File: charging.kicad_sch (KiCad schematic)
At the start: 23 parts, among them IC1 APX803S-31SA-7, J2 10164359-00011LF, Q1 BSS806NEH6327XTSA1, Q2 DMG2305UX, SW3 Power Switch, U3 MIC5365-3.3YC5-TR, U4 MCP73832

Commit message: added test points
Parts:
- added TP7: VBUS, TestPoint:TestPoint_Pad_1.0x1.0mm, symbol Connector:TestPoint
- added TP8: BATT, TestPoint:TestPoint_Pad_1.0x1.0mm, symbol Connector:TestPoint
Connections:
- net +BATT: now also TP8.1
- net VBUS: now also TP7.1
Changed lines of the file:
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@@
 	)
 	(junction
+		(at 66.04 68.58)
+		(diameter 0)
+		(color 0 0 0 0)
+	)
+	(junction
 		(at 59.69 128.27)
 		(diameter 0)
@@
 	)
 	(symbol
+		(lib_id "Connector:TestPoint")
+		(at 66.04 68.58 270)
+		(unit 1)
+		(exclude_from_sim no)
+		(in_bom yes)
+		(on_board yes)
+		(dnp no)
+		(fields_autoplaced yes)
+		(property "Reference" "TP7"
+			(at 71.12 67.3099 90)
+			(effects
+				(font
+					(size 1.27 1.27)
+				)
+				(justify left)
+			)
+		)
+		(property "Value" "VBUS"
+			(at 71.12 69.8499 90)
+			(effects
+				(font
+					(size 1.27 1.27)
+				)
+				(justify left)
+			)
+		)
+		(property "Footprint" "TestPoint:TestPoint_Pad_1.0x1.0mm"
+			(at 66.04 73.66 0)
+			(effects
+				(font
+					(size 1.27 1.27)
+				)
+				(hide yes)
+			)
+		)
+		(property "Datasheet" "~"
+			(at 66.04 73.66 0)
+			(effects
+				(font
+					(size 1.27 1.27)
+				)
+				(hide yes)
+			)
+		)
+		(property "Description" "test point"
+			(at 66.04 68.58 0)
+			(effects
+				(font
+					(size 1.27 1.27)
+				)
+				(hide yes)
+			)
+		)
+		(pin "1"
+		)
+		(instances
+			(project ""
+				(path "/5c9eb70e-53a3-4f57-8f37-8853f9cac53c/b9b17dec-f84f-4841-bdb5-cbe0cc549f61"
+					(reference "TP7")
+					(unit 1)
+				)
+			)
+		)
+	)
+	(symbol
 		(lib_id "MIC5365-3.3YC5-TR:MIC5365-3.3YC5-TR")
 		(at 184.15 77.47 0)
@@
 					(unit 1)
 				)
+			)
+		)
+	)
+	(symbol
+		(lib_id "Connector:TestPoint")
+		(at 31.75 111.76 90)
+		(unit 1)
+		(exclude_from_sim no)
+		(in_bom yes)
+		(on_board yes)
+		(dnp no)
+		(fields_autoplaced yes)
+		(property "Reference" "TP8"
+			(at 28.448 106.68 90)
+			(effects
+				(font
+					(size 1.27 1.27)
+				)
+			)
+		)
+		(property "Value" "BATT"
+			(at 28.448 109.22 90)
+			(effects
+				(font
+					(size 1.27 1.27)
+				)
+			)
+		)
+		(property "Footprint" "TestPoint:TestPoint_Pad_1.0x1.0mm"
+			(at 31.75 106.68 0)
+			(effects
+				(font
+					(size 1.27 1.27)
+				)
+				(hide yes)
+			)
+		)
+		(property "Datasheet" "~"
+			(at 31.75 106.68 0)
+			(effects
+				(font
+					(size 1.27 1.27)
+				)
+				(hide yes)
+			)
+		)
+		(property "Description" "test point"
+			(at 31.75 111.76 0)
+			(effects
+				(font
+					(size 1.27 1.27)
+				)
+				(hide yes)
+			)
+		)
+		(pin "1"
+		)
+		(instances
+			(project "bookbuddy_pcb"
+				(path "/5c9eb70e-53a3-4f57-8f37-8853f9cac53c/b9b17dec-f84f-4841-bdb5-cbe0cc549f61"
+					(reference "TP8")
+					(unit 1)
+				)

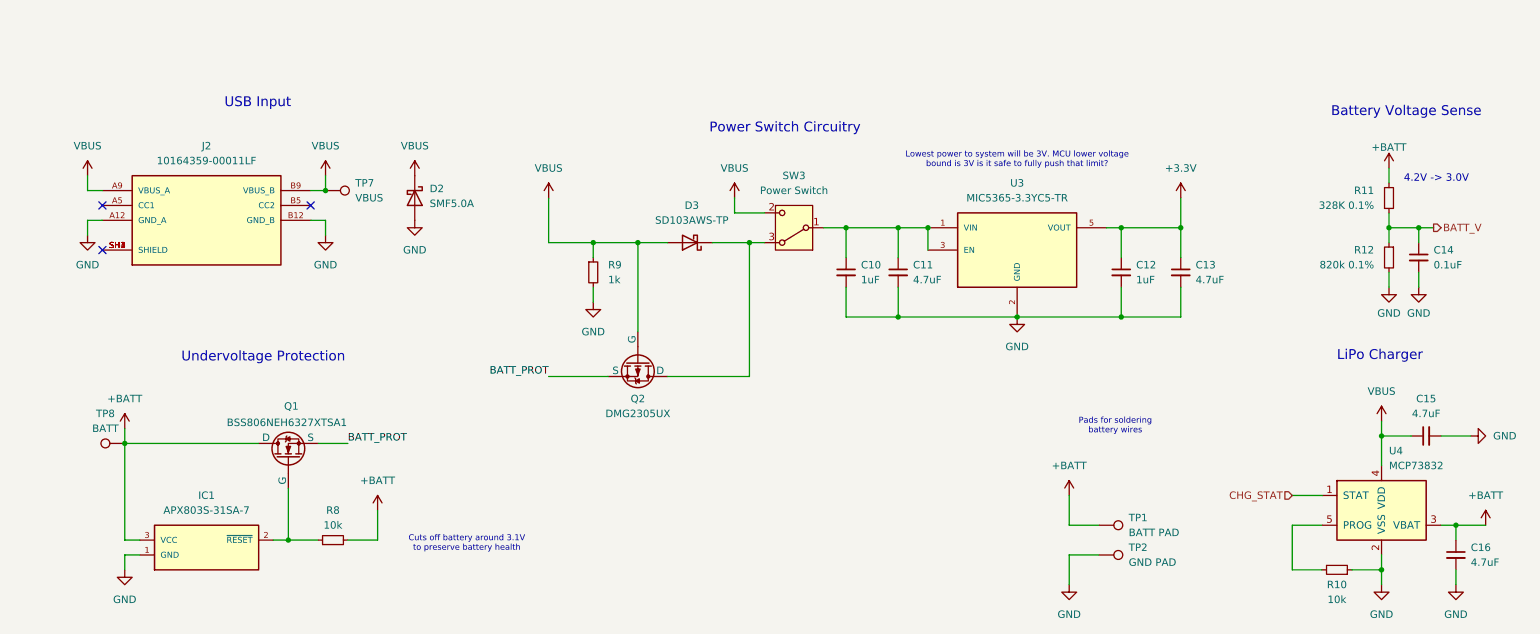
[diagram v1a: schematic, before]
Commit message: Made changes up to diode logic
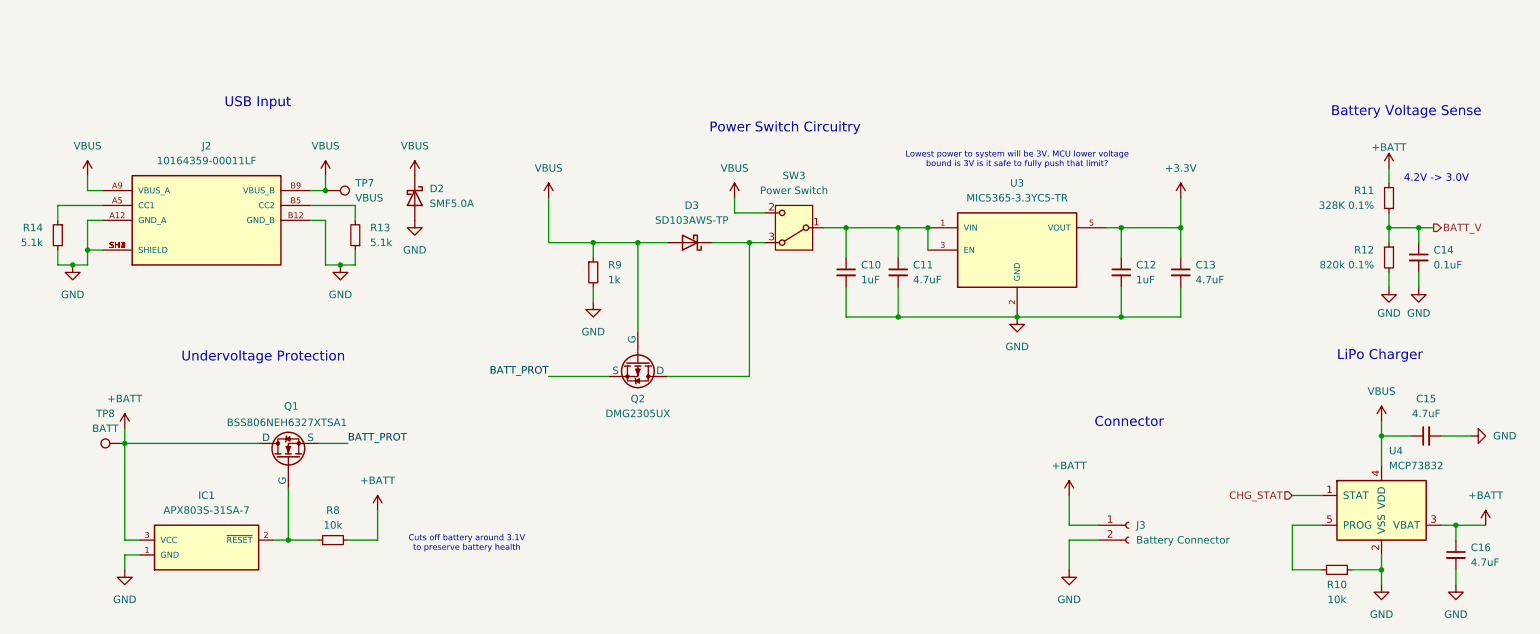
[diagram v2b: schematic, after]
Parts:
- removed TP1: BATT PAD, TestPoint:TestPoint_Pad_1.5x1.5mm, symbol Connector:TestPoint
- removed TP2: GND PAD, TestPoint:TestPoint_Pad_1.5x1.5mm, symbol Connector:TestPoint
- added J3: Battery Connector, bookbuddy:JST_S2B-PH-K-S_LF__SN_, symbol Connector:Conn_01x02_Socket
- added R13, R14: 5.1k, Resistor_SMD:R_0603_1608Metric_Pad0.98x0.95mm_HandSolder, symbol Device:R_Small
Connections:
- net +BATT: now also J3.1 (Pin_1)
- net GND: now also J2.SH1 (SHIELD), J2.SH2 (SHIELD), J2.SH3 (SHIELD), J2.SH4 (SHIELD), J3.2 (Pin_2), R13.1, R14.2
- net at J2.A5 (CC1): now also R14.1
- net at J2.B5 (CC2): now also R13.2
- no-connect marks 3 -> 0
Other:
- note added: "Connector"
- note removed: "Pads for soldering battery wires"

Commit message: made remaining changes to the schematic
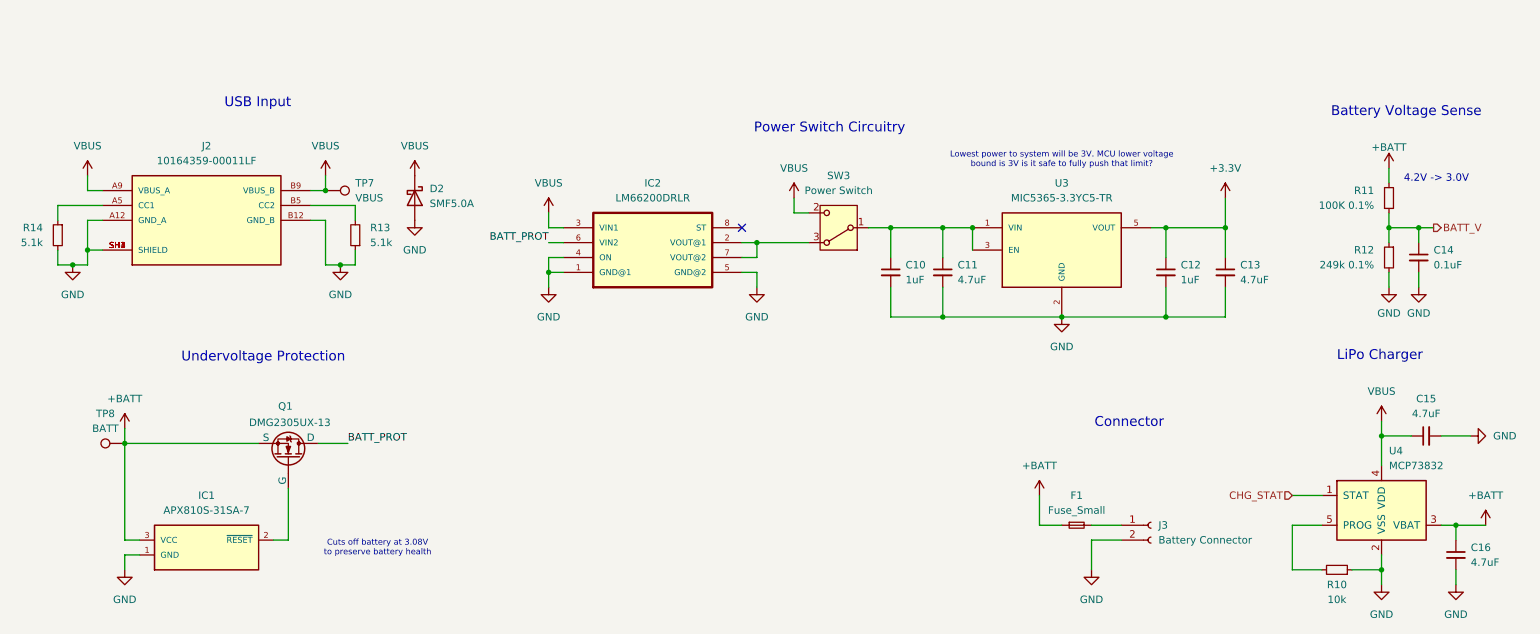
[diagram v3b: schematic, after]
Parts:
- removed D3: SD103AWS-TP, Diode_SMD:D_SOD-323, symbol Device:D_Schottky
- removed Q2: DMG2305UX, Package_TO_SOT_SMD:SOT-23-3, symbol Simulation_SPICE:PMOS
- removed R8: 10k, Resistor_SMD:R_0603_1608Metric_Pad0.98x0.95mm_HandSolder, symbol Device:R_Small
- removed R9: 1k, Resistor_SMD:R_0603_1608Metric_Pad0.98x0.95mm_HandSolder, symbol Device:R_Small
- added F1: Fuse_Small, symbol Device:Fuse_Small
- added IC2: LM66200DRLR, bookbuddy:SOT8, symbol LM66200DRLR:LM66200DRLR
- IC1: value APX803S-31SA-7 -> APX810S-31SA-7
- Q1: value BSS806NEH6327XTSA1 -> DMG2305UX-13
- R11: value 328K 0.1% -> 100K 0.1%
- R12: value 820k 0.1% -> 249k 0.1%
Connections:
- net +BATT: now also Q1.3 (S), F1.1; no longer J3.1 (Pin_1), Q1.1 (D)
- net BATT_PROT: now also Q1.1 (D), IC2.6 (VIN2); no longer Q1.3 (S)
- net GND: now also IC2.1 (GND@1), IC2.4 (ON), IC2.5 (GND@2)
- net VBUS: now also IC2.3 (VIN1)
- net at SW3.3 (A): now also IC2.2 (VOUT@1), IC2.7 (VOUT@2)
- new net: F1.2, J3.1 (Pin_1)
- no-connect marks 0 -> 1
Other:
- note added: "Cuts off battery at 3.08V to preserve battery health"
- note removed: "Cuts off battery around 3.1V to preserve battery health"
- moved on the sheet: C10, C11, C12, C13, J3, Q1, SW3, U3

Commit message: addressed Craig's comments
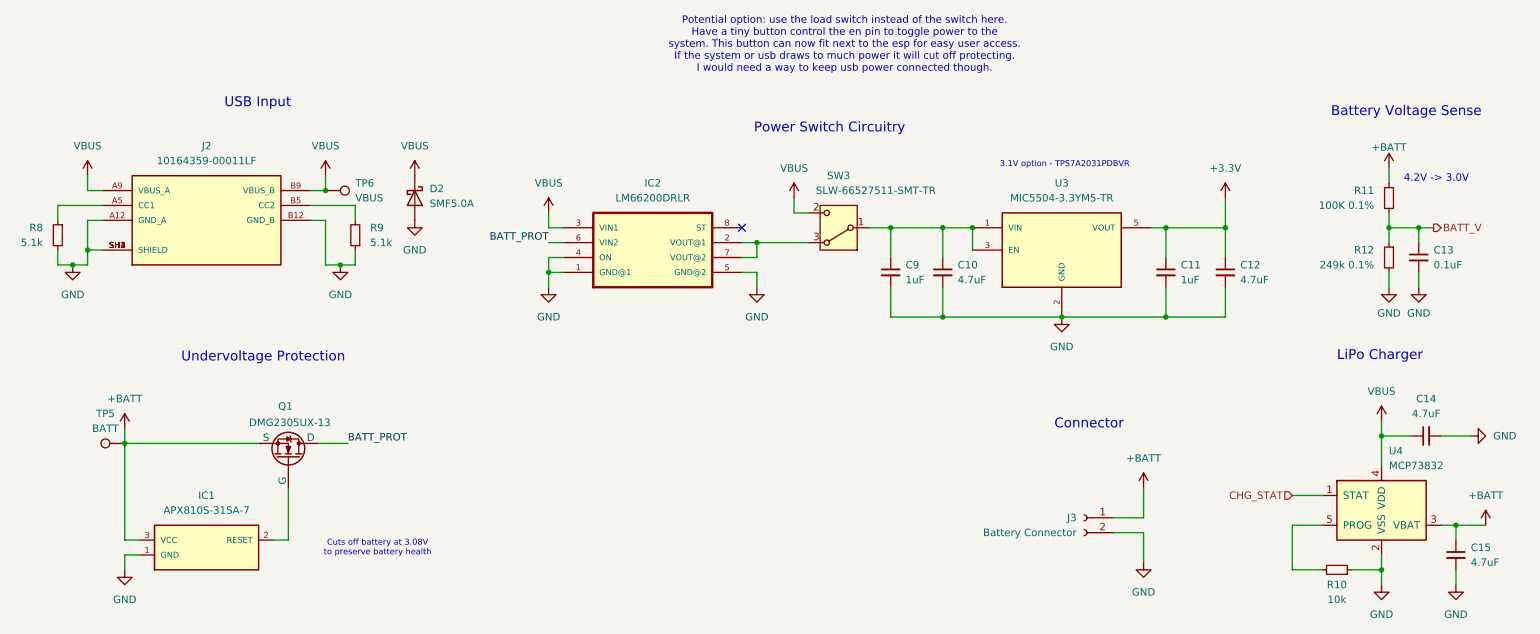
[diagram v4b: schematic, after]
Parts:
- removed F1: Fuse_Small, symbol Device:Fuse_Small
- SW3: value Power Switch -> SLW-66527511-SMT-TR; footprint bookbuddy:CUS-12B -> bookbuddy:SW_SLW-66527511-SMT-TR
- U3: value MIC5365-3.3YC5-TR -> MIC5504-3.3YM5-TR; footprint bookbuddy:SOT65P210X110-5N -> Package_TO_SOT_SMD:SOT-23-5_HandSoldering
- renumbered C11 to C10, C12 to C11, C13 to C12, C14 to C13, C15 to C14, C16 to C15, C10 to C9, R14 to R8, R13 to R9, TP8 to TP5, TP7 to TP6
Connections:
- net +BATT: now also J3.1 (Pin_1)
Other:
- note added: "3.1V option - TPS7A2031PDBVR"
- note added: "Potential option: use the load switch instead of the switch here. Have a tiny button control the en pin to toggle power to the system. This button can now fit next to the esp for easy user access. If the system or usb draws to much power it will cut off protecting. I would need a way to keep usb power connected though."
- note removed: "Lowest power to system will be 3V. MCU lower voltage bound is 3V is it safe to fully push that limit?"
- moved on the sheet: J3

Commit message: Added fuse
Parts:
- added F1: ERB-RD0R50X, bookbuddy:FUSC0402X49N, symbol Device:Fuse_Small
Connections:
- net +BATT: now also F1.2; no longer J3.1 (Pin_1)
- new net: F1.1, J3.1 (Pin_1)
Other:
- note added: "0.5A Rating"
- moved on the sheet: J3
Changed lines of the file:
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@@
 	(wire
 		(pts
-			(xy 205.74 127) (xy 205.74 132.08)
+			(xy 198.12 127) (xy 198.12 132.08)
 		)
 		(stroke
@@
 	(wire
 		(pts
-			(xy 200.66 127) (xy 205.74 127)
+			(xy 193.04 127) (xy 198.12 127)
+		)
+		(stroke
+			(width 0)
+			(type default)
+		)
+	)
+	(wire
+		(pts
+			(xy 193.04 124.46) (xy 195.58 124.46)
 		)
 		(stroke
@@
 		)
 	)
+	(text "0.5A Rating"
+		(exclude_from_sim no)
+		(at 187.198 117.856 0)
+		(effects
+			(font
+				(size 1.27 1.27)
+			)
+		)
+	)
 	(text "Power Switch Circuitry"
 		(exclude_from_sim no)
@@
 	(symbol
 		(lib_id "power:GND")
-		(at 205.74 132.08 0)
+		(at 198.12 132.08 0)
 		(mirror y)
 		(unit 1)
@@
 		(fields_autoplaced yes)
 		(property "Reference" "#PWR041"
-			(at 205.74 138.43 0)
+			(at 198.12 138.43 0)
 			(effects
 				(font
@@
 		)
 		(property "Value" "GND"
-			(at 205.74 137.16 0)
+			(at 198.12 137.16 0)
 			(effects
 				(font
@@
 		)
 		(property "Footprint" ""
-			(at 205.74 132.08 0)
+			(at 198.12 132.08 0)
 			(effects
 				(font
@@
 		)
 		(property "Datasheet" ""
-			(at 205.74 132.08 0)
+			(at 198.12 132.08 0)
 			(effects
 				(font
@@
 		)
 		(property "Description" "Power symbol creates a global label with name \"GND\" , ground"
-			(at 205.74 132.08 0)
+			(at 198.12 132.08 0)
 			(effects
 				(font
@@
 	(symbol
 		(lib_id "Connector:Conn_01x02_Socket")
-		(at 195.58 124.46 0)
+		(at 187.96 124.46 0)
 		(mirror y)
 		(unit 1)
@@
 		(fields_autoplaced yes)
 		(property "Reference" "J3"
-			(at 194.31 124.4599 0)
+			(at 186.69 124.4599 0)
 			(effects
 				(font
@@
 		)
 		(property "Value" "Battery Connector"
-			(at 194.31 126.9999 0)
+			(at 186.69 126.9999 0)
 			(effects
 				(font
@@
 		)
 		(property "Footprint" "bookbuddy:JST_S2B-PH-K-S_LF__SN_"
-			(at 195.58 124.46 0)
+			(at 187.96 124.46 0)
 			(effects
 				(font
@@
 		)
 		(property "Datasheet" "~"
-			(at 195.58 124.46 0)
+			(at 187.96 124.46 0)
 			(effects
 				(font
@@
 		)
 		(property "Description" "Generic connector, single row, 01x02, script generated"
-			(at 195.58 124.46 0)
+			(at 187.96 124.46 0)
 			(effects
 				(font
@@
 					(unit 1)
 				)
+			)
+		)
+	)
+	(symbol
+		(lib_id "Device:Fuse_Small")
+		(at 198.12 124.46 0)
+		(unit 1)
+		(exclude_from_sim no)
+		(in_bom yes)
+		(on_board yes)
+		(dnp no)
+		(fields_autoplaced yes)
+		(property "Reference" "F1"
+			(at 198.12 119.38 0)
+			(effects
+				(font
+					(size 1.27 1.27)
+				)
+			)
+		)
+		(property "Value" "ERB-RD0R50X"
+			(at 198.12 121.92 0)
+			(effects
+				(font
+					(size 1.27 1.27)
+				)
+			)
+		)
+		(property "Footprint" "bookbuddy:FUSC0402X49N"
+			(at 198.12 124.46 0)
+			(effects
+				(font
+					(size 1.27 1.27)
+				)
+				(hide yes)
+			)
+		)
+		(property "Datasheet" "~"
+			(at 198.12 124.46 0)
+			(effects
+				(font
+					(size 1.27 1.27)
+				)
+				(hide yes)
+			)
+		)
+		(property "Description" "Fuse, small symbol"
+			(at 198.12 124.46 0)
+			(effects
+				(font
+					(size 1.27 1.27)
+				)
+				(hide yes)
+			)
+		)
+		(pin "1"
+		)
+		(pin "2"
+		)
+		(instances
+			(project ""
+				(path "/5c9eb70e-53a3-4f57-8f37-8853f9cac53c/b9b17dec-f84f-4841-bdb5-cbe0cc549f61"
+					(reference "F1")
+					(unit 1)
+				)

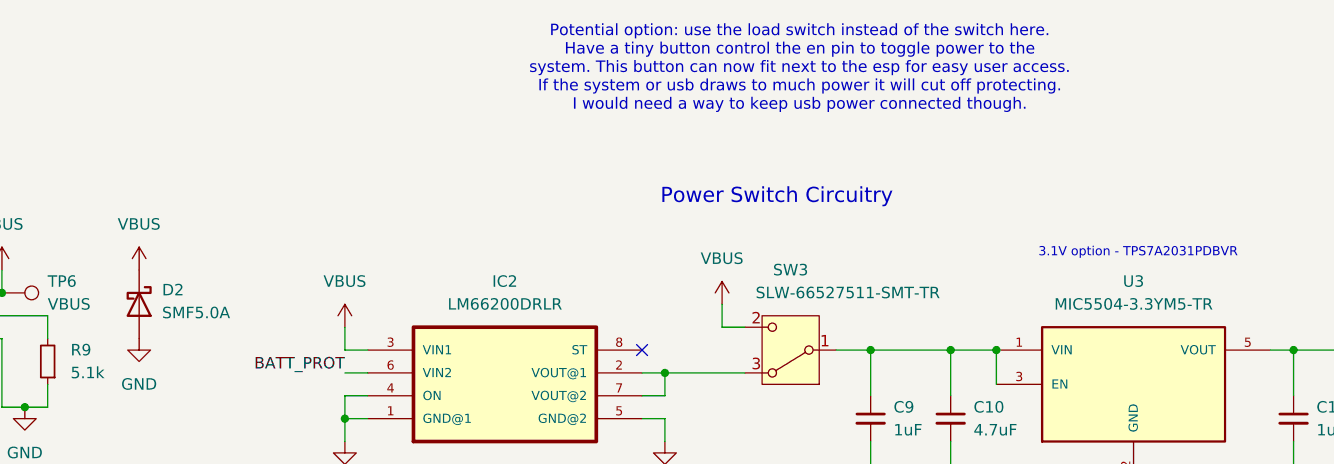
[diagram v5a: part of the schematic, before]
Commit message: finished routing the pcb
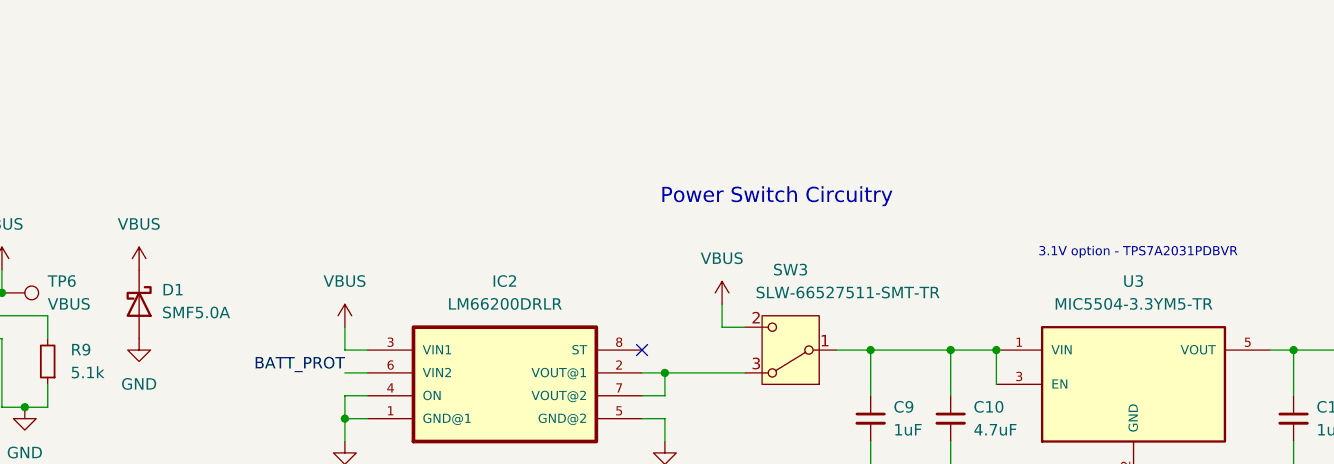
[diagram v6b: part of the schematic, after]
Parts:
- renumbered D2 to D1
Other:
- note removed: "Potential option: use the load switch instead of the switch here. Have a tiny button control the en pin to toggle power to the system. This button can now fit next to the esp for easy user access. If the system or usb draws to much power it will cut off protecting. I would need a way to keep usb power connected though."
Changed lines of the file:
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@@
-		)
-	)
-	(text "Potential option: use the load switch instead of the switch here.\nHave a tiny button control the en pin to toggle power to the\nsystem. This button can now fit next to the esp for easy user access.\nIf the system or usb draws to much power it will cut off protecting.\nI would need a way to keep usb power connected though.\n"
-		(exclude_from_sim no)
-		(at 154.686 43.688 0)
-		(effects
-			(font
-				(size 1.27 1.27)
-			)
 		)
 	)
@@
 		(dnp no)
 		(fields_autoplaced yes)
-		(property "Reference" "D2"
+		(property "Reference" "D1"
 			(at 83.82 68.2624 90)
 			(effects
@@
 			(project "bookbuddy_pcb"
 				(path "/5c9eb70e-53a3-4f57-8f37-8853f9cac53c/b9b17dec-f84f-4841-bdb5-cbe0cc549f61"
-					(reference "D2")
-					(unit 1)
-				)
+					(reference "D1")
+					(unit 1)
+				)
